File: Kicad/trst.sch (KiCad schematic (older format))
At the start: 25 parts, among them CN2 , J1 Conn_02x30_Odd_Even, U1 MC88916, U11 PALCE16V8H, U21 DM74AS646, U22 DM74AS646, U23 DM74AS646, U24 DM74AS646, U3 PALCE20V8H, U4 MC68040, U6 MACH130, U8 MACH110, U9 PAL22V10, X1 GTXO-S14V

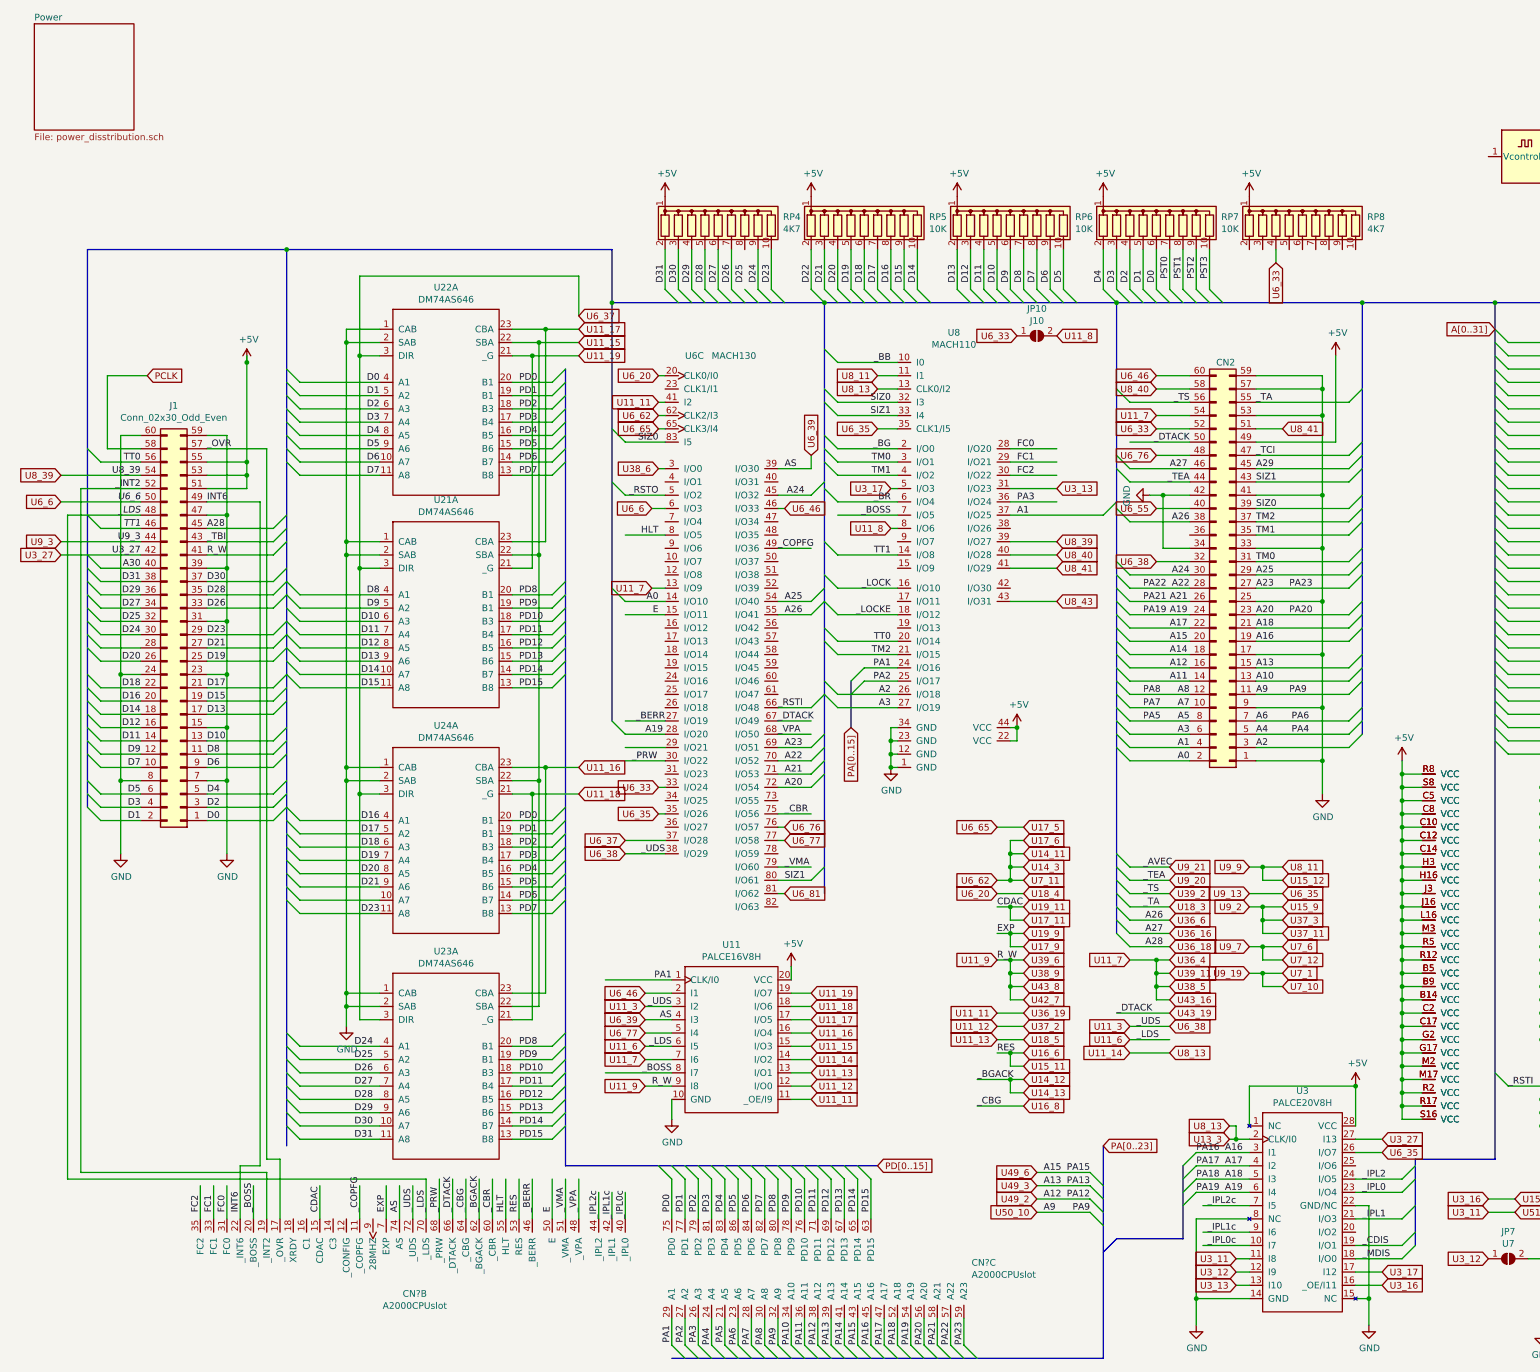
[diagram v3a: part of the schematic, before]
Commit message: glue logic and dram buss
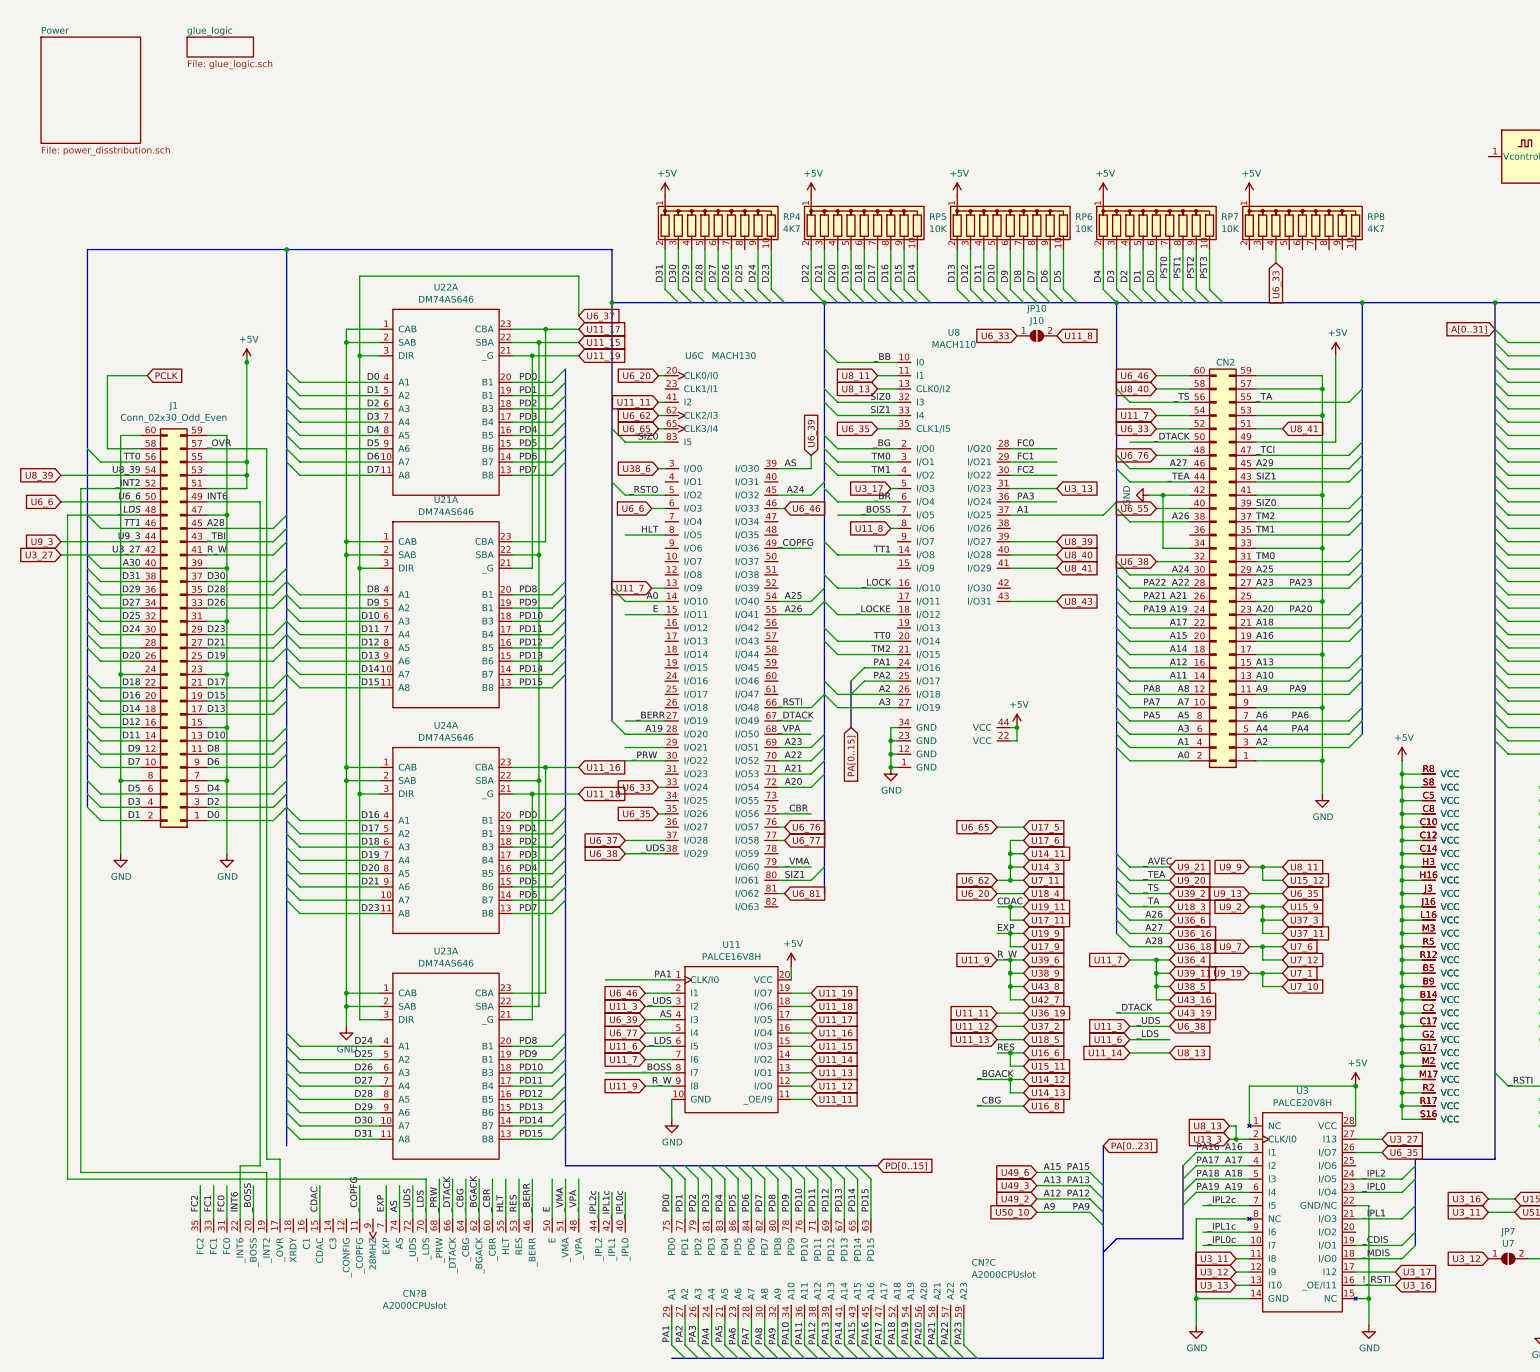
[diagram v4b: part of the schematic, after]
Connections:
- net labels added: !_RSTI
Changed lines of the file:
@@
 $Descr User 17000 11000
 encoding utf-8
-Sheet 1 2
+Sheet 1 3
 Title ""
 Date ""
@@
 $EndComp
 $Sheet
-S 550  550  750  800
+S 600  650  750  800
 U 5D6ED44C
 F0 "Power" 50
@@
 Wire Wire Line
 	7050 4050 7000 4050
-Text GLabel 10700 9950 2    50   Input ~ 0
-U3_17
-Wire Wire Line
-	10700 9950 10500 9950
 Wire Wire Line
 	7050 3100 6600 3100
@@
 Text GLabel 11700 9400 2    50   Input ~ 0
 U15_2
-Text GLabel 10700 10050 2    50   Input ~ 0
+Text GLabel 10800 10050 2    50   Input ~ 0
 U3_16
 Wire Wire Line
-	10700 10050 10500 10050
+	10800 10050 10500 10050
 Text GLabel 11500 9400 0    50   Input ~ 0
 U3_16
@@
 Wire Wire Line
 	16250 7950 16050 7950
+$Sheet
+S 1700 650  500  150
+U 5D991873
+F0 "glue_logic" 50
+F1 "glue_logic.sch" 50
+$EndSheet
+Text Label 10550 10050 0    50   ~ 0
+!_RSTI
+Text GLabel 10800 9950 2    50   Input ~ 0
+U3_17
+Wire Wire Line
+	10800 9950 10500 9950
 Wire Wire Line
 	6600 5600 7050 5600

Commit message: few glued wires
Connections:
- net labels added: U14_2, U6_73
- wire segments 874 -> 876
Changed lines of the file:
@@
 	10800 9950 10500 9950
+Wire Wire Line
+	5300 6400 5250 6400
+Text GLabel 5250 6400 0    50   Input ~ 0
+U14_2
+Text GLabel 6200 6400 2    50   Input ~ 0
+U6_73
+Wire Wire Line
+	6200 6400 6150 6400
 Wire Wire Line
 	6600 5600 7050 5600

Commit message: nothing special
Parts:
- added R26, R27: 220R, symbol Device:R
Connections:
- net labels added: U12_5, U12_6, U12_9, U13_11, U8_35
- wire segments 876 -> 887
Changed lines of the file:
@@
 Text Label 9300 9050 0    50   ~ 0
 PA16
-Text GLabel 9550 8950 0    50   Input ~ 0
+Text GLabel 8800 8550 0    50   Input ~ 0
 U13_3
-Wire Wire Line
-	9550 8950 9600 8950
 Wire Wire Line
 	9700 9350 9300 9350
@@
 Wire Wire Line
 	8800 8300 9100 8300
-Text GLabel 9550 8850 0    50   Input ~ 0
+Text GLabel 8800 8450 0    50   Input ~ 0
 U8_13
 Wire Wire Line
-	9550 8850 9600 8850
-Wire Wire Line
-	9600 8850 9600 8950
-Connection ~ 9600 8950
-Wire Wire Line
-	9600 8950 9700 8950
+	8800 8450 8900 8450
+Wire Wire Line
+	9000 8450 9000 8700
 $Comp
 L New_Library_0:PALCE16V8H U11
@@
 Wire Wire Line
 	6900 3200 7050 3200
-Text GLabel 6900 3600 0    50   Input ~ 0
-U6_35
 Wire Wire Line
 	6900 3600 7050 3600
@@
 Wire Wire Line
 	6200 6400 6150 6400
+Text GLabel 6200 5600 2    50   Input ~ 0
+U12_5
+Wire Wire Line
+	6200 5600 6150 5600
+Text GLabel 6200 5300 2    50   Input ~ 0
+U12_6
+Wire Wire Line
+	6200 5300 6150 5300
+Text GLabel 6200 5400 2    50   Input ~ 0
+U12_9
+Wire Wire Line
+	6200 5400 6150 5400
+Wire Wire Line
+	8800 8550 8900 8550
+Wire Wire Line
+	8900 8550 8900 8450
+Connection ~ 8900 8450
+Wire Wire Line
+	8900 8450 9000 8450
+Wire Wire Line
+	9550 8950 9550 8700
+Wire Wire Line
+	9550 8950 9700 8950
+Wire Wire Line
+	9000 8700 9100 8700
+$Comp
+L Device:R R26
+U 1 1 5E34955E
+P 9100 8550
+F 0 "R26" H 9170 8596 50  0000 L CNN
+F 1 "220R" H 9170 8505 50  0000 L CNN
+F 2 "" V 9030 8550 50  0001 C CNN
+F 3 "~" H 9100 8550 50  0001 C CNN
+	1    9100 8550
+	1    0    0    -1
+$EndComp
+$Comp
+L Device:R R27
+U 1 1 5E349A55
+P 9100 8850
+F 0 "R27" H 9170 8896 50  0000 L CNN
+F 1 "220R" H 9170 8805 50  0000 L CNN
+F 2 "" V 9030 8850 50  0001 C CNN
+F 3 "~" H 9100 8850 50  0001 C CNN
+	1    9100 8850
+	1    0    0    -1
+$EndComp
+Connection ~ 9100 8700
+Wire Wire Line
+	9100 8700 9550 8700
+$Comp
+L power:+5V #PWR?
+U 1 1 5E34A208
+P 9550 8400
+F 0 "#PWR?" H 9550 8250 50  0001 C CNN
+F 1 "+5V" H 9565 8573 50  0000 C CNN
+F 2 "" H 9550 8400 50  0001 C CNN
+F 3 "" H 9550 8400 50  0001 C CNN
+	1    9550 8400
+	1    0    0    -1
+$EndComp
+Wire Wire Line
+	9100 8400 9550 8400
+$Comp
+L power:GND #PWR?
+U 1 1 5E443443
+P 9100 9000
+F 0 "#PWR?" H 9100 8750 50  0001 C CNN
+F 1 "GND" H 9105 8827 50  0000 C CNN
+F 2 "" H 9100 9000 50  0001 C CNN
+F 3 "" H 9100 9000 50  0001 C CNN
+	1    9100 9000
+	1    0    0    -1
+$EndComp
+Text GLabel 6900 3600 0    50   Input ~ 0
+U8_35
+Text GLabel 8800 8650 0    50   Input ~ 0
+U13_11
+Wire Wire Line
+	8800 8650 8900 8650
+Wire Wire Line
+	8900 8650 8900 8550
 Wire Wire Line
 	6600 5600 7050 5600
@@
 Wire Bus Line
 	2450 2250 2450 9000
+Connection ~ 8900 8550
 $EndSCHEMATC

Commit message: some dram schematics
dram section, data and address bus
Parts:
- added JP16: J16, symbol Jumper:SolderJumper_2_Open
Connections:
- wire segments 887 -> 889
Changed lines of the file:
@@
 $Descr User 17000 11000
 encoding utf-8
-Sheet 1 3
+Sheet 1 4
 Title ""
 Date ""
@@
 Text Label 4000 9500 1    50   ~ 0
 _CBR
-Text Label 6200 6500 0    50   ~ 0
+Text Label 6200 5100 0    50   ~ 0
 _CBR
 Wire Wire Line
-	6150 6500 6400 6500
-Wire Wire Line
 	3900 9550 3900 9250
 Text Label 3900 9500 1    50   ~ 0
@@
 Wire Wire Line
 	8900 8650 8900 8550
+Connection ~ 8900 8550
+Wire Wire Line
+	6150 5100 6400 5100
+Wire Wire Line
+	6150 6500 6700 6500
+$Comp
+L Jumper:SolderJumper_2_Open JP16
+U 1 1 5E21EBD7
+P 6850 6500
+F 0 "JP16" H 6850 6705 50  0000 C CNN
+F 1 "J16" H 6850 6614 50  0000 C CNN
+F 2 "" H 6850 6500 50  0001 C CNN
+F 3 "~" H 6850 6500 50  0001 C CNN
+	1    6850 6500
+	1    0    0    -1
+$EndComp
+$Comp
+L power:GND #PWR?
+U 1 1 5E31C40E
+P 7000 6600
+F 0 "#PWR?" H 7000 6350 50  0001 C CNN
+F 1 "GND" H 7005 6427 50  0000 C CNN
+F 2 "" H 7000 6600 50  0001 C CNN
+F 3 "" H 7000 6600 50  0001 C CNN
+	1    7000 6600
+	1    0    0    -1
+$EndComp
+Wire Wire Line
+	7000 6600 7000 6500
 Wire Wire Line
 	6600 5600 7050 5600
@@
 Wire Bus Line
 	2450 2250 2450 9000
-Connection ~ 8900 8550
+$Sheet
+S 3000 800  800  200
+U 5EABF28F
+F0 "dram_part" 50
+F1 "dram.sch" 50
+$EndSheet
 $EndSCHEMATC
